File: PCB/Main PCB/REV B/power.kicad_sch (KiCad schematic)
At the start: 16 parts, among them U5 TPS2115APWR, U6 AMS1117-3.3

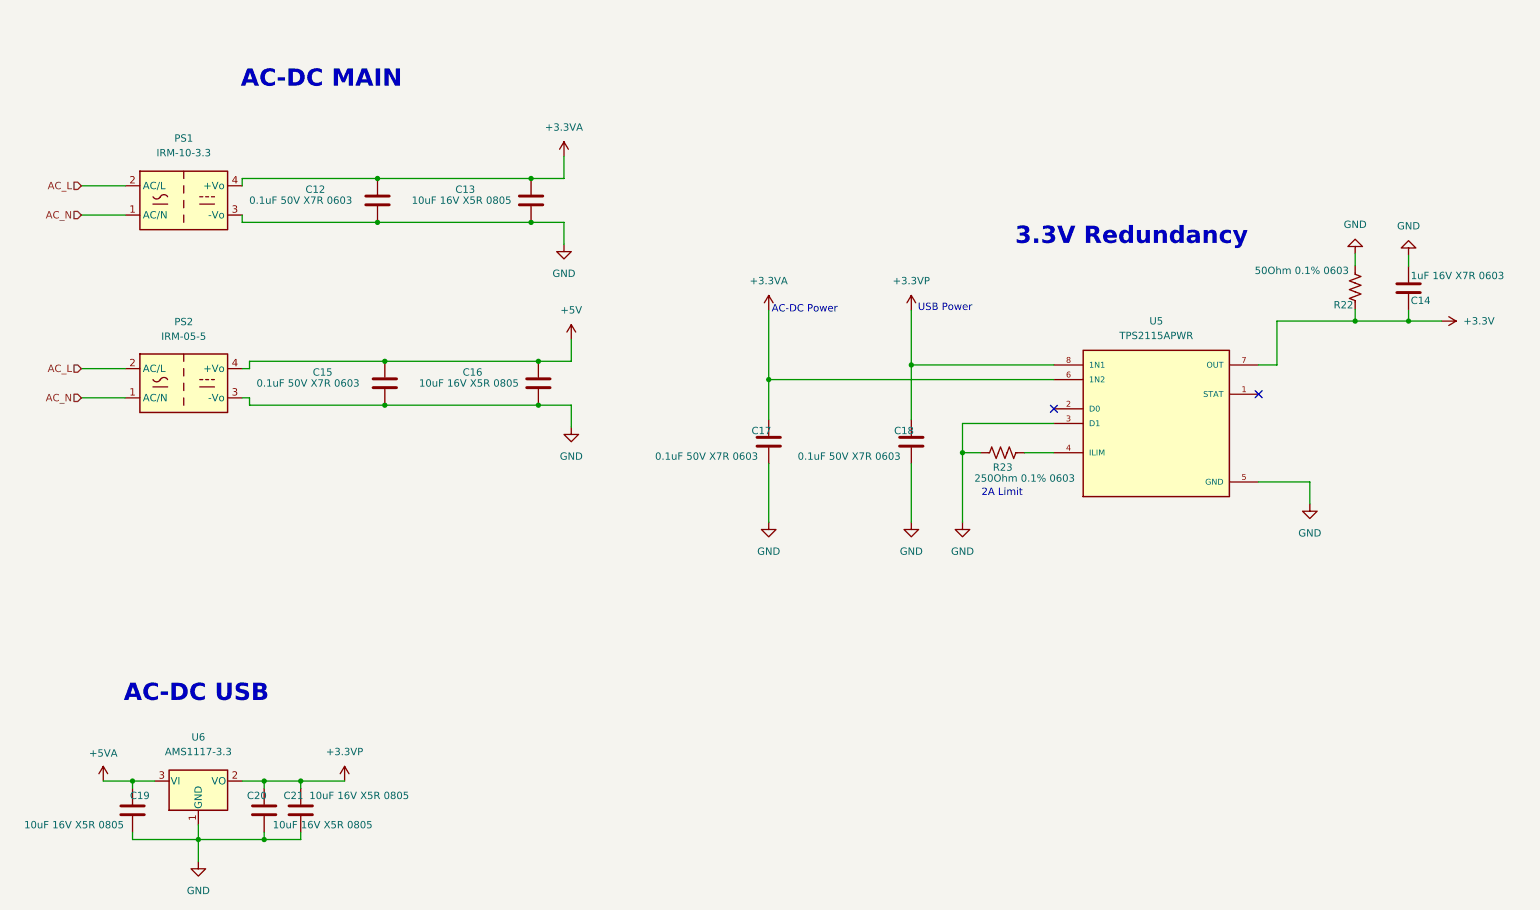
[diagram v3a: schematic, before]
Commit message: PCB schematic updates, Change to smaller thermocouple mux
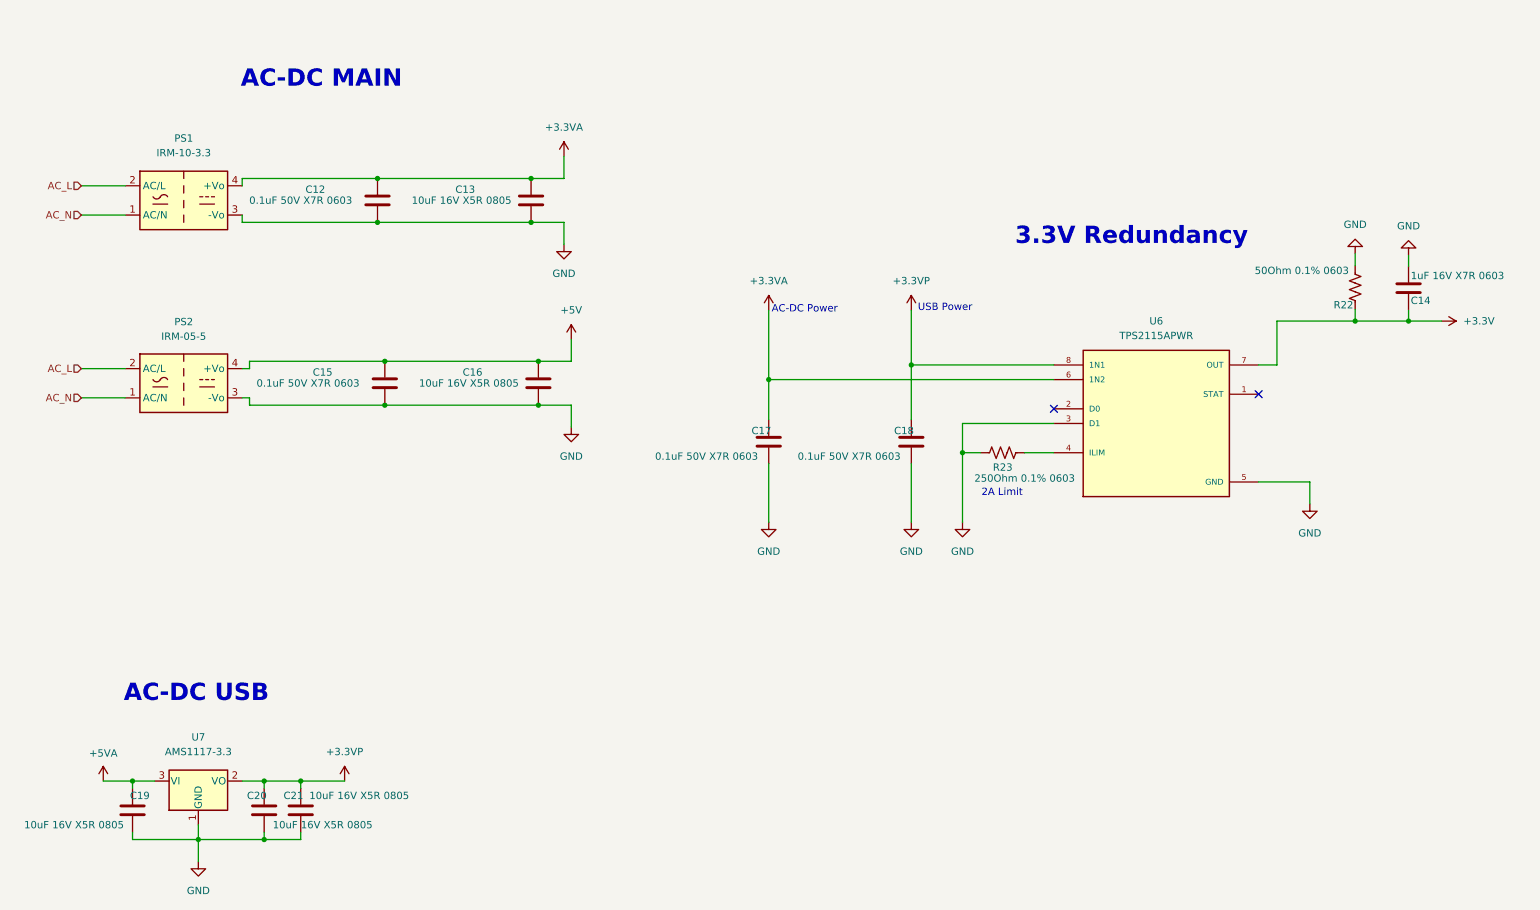
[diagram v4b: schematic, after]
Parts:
- renumbered U5 to U6, U6 to U7
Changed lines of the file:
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@@
   (symbol (lib_id "TPS2115APWR:TPS2115APWR") (at 218.694 92.329 0) (unit 1)
     (in_bom yes) (on_board yes) (fields_autoplaced)
-    (property "Reference" "U5" (id 0) (at 218.694 74.549 0))
+    (property "Reference" "U6" (id 0) (at 218.694 74.549 0))
     (property "Value" "TPS2115APWR" (id 1) (at 218.694 77.089 0))
     (property "Footprint" "Customs Smoker:PW8-M" (id 2) (at 218.694 92.329 0)
@@
   (symbol (lib_id "power:+3.3VP") (at 176.149 72.644 0) (unit 1)
     (in_bom yes) (on_board yes) (fields_autoplaced)
-    (property "Reference" "#PWR058" (id 0) (at 179.959 73.914 0)
+    (property "Reference" "#PWR057" (id 0) (at 179.959 73.914 0)
       (effects (font (size 1.27 1.27)) hide)
     )
@@
   (symbol (lib_id "power:GND") (at 52.324 168.402 0) (unit 1)
     (in_bom yes) (on_board yes)
-    (property "Reference" "#PWR068" (id 0) (at 52.324 174.752 0)
+    (property "Reference" "#PWR067" (id 0) (at 52.324 174.752 0)
       (effects (font (size 1.27 1.27)) hide)
     )
@@
   (symbol (lib_id "power:GND") (at 151.384 109.474 0) (unit 1)
     (in_bom yes) (on_board yes) (fields_autoplaced)
-    (property "Reference" "#PWR063" (id 0) (at 151.384 115.824 0)
+    (property "Reference" "#PWR062" (id 0) (at 151.384 115.824 0)
       (effects (font (size 1.27 1.27)) hide)
     )
@@
   (symbol (lib_id "power:GND") (at 185.039 109.474 0) (unit 1)
     (in_bom yes) (on_board yes) (fields_autoplaced)
-    (property "Reference" "#PWR065" (id 0) (at 185.039 115.824 0)
+    (property "Reference" "#PWR064" (id 0) (at 185.039 115.824 0)
       (effects (font (size 1.27 1.27)) hide)
     )
@@
   (symbol (lib_id "power:+3.3V") (at 268.224 74.549 270) (unit 1)
     (in_bom yes) (on_board yes) (fields_autoplaced)
-    (property "Reference" "#PWR059" (id 0) (at 264.414 74.549 0)
+    (property "Reference" "#PWR058" (id 0) (at 264.414 74.549 0)
       (effects (font (size 1.27 1.27)) hide)
     )
@@
   (symbol (lib_id "power:GND") (at 117.094 92.964 0) (unit 1)
     (in_bom yes) (on_board yes)
-    (property "Reference" "#PWR061" (id 0) (at 117.094 99.314 0)
+    (property "Reference" "#PWR060" (id 0) (at 117.094 99.314 0)
       (effects (font (size 1.27 1.27)) hide)
     )
@@
   (symbol (lib_id "power:+3.3VA") (at 151.384 72.644 0) (unit 1)
     (in_bom yes) (on_board yes) (fields_autoplaced)
-    (property "Reference" "#PWR057" (id 0) (at 151.384 76.454 0)
+    (property "Reference" "#PWR056" (id 0) (at 151.384 76.454 0)
       (effects (font (size 1.27 1.27)) hide)
     )
@@
   (symbol (lib_id "power:GND") (at 115.824 61.214 0) (unit 1)
     (in_bom yes) (on_board yes)
-    (property "Reference" "#PWR054" (id 0) (at 115.824 67.564 0)
+    (property "Reference" "#PWR053" (id 0) (at 115.824 67.564 0)
       (effects (font (size 1.27 1.27)) hide)
     )
@@
   (symbol (lib_id "power:GND") (at 253.238 62.865 180) (unit 1)
     (in_bom yes) (on_board yes) (fields_autoplaced)
-    (property "Reference" "#PWR055" (id 0) (at 253.238 56.515 0)
+    (property "Reference" "#PWR054" (id 0) (at 253.238 56.515 0)
       (effects (font (size 1.27 1.27)) hide)
     )
@@
   (symbol (lib_id "power:+3.3VP") (at 77.724 154.432 0) (unit 1)
     (in_bom yes) (on_board yes) (fields_autoplaced)
-    (property "Reference" "#PWR067" (id 0) (at 81.534 155.702 0)
+    (property "Reference" "#PWR066" (id 0) (at 81.534 155.702 0)
       (effects (font (size 1.27 1.27)) hide)
     )
@@
   (symbol (lib_id "power:GND") (at 262.509 63.119 180) (unit 1)
     (in_bom yes) (on_board yes) (fields_autoplaced)
-    (property "Reference" "#PWR056" (id 0) (at 262.509 56.769 0)
+    (property "Reference" "#PWR055" (id 0) (at 262.509 56.769 0)
       (effects (font (size 1.27 1.27)) hide)
     )
@@
   (symbol (lib_id "Regulator_Linear:AMS1117-3.3") (at 52.324 154.432 0) (unit 1)
     (in_bom yes) (on_board yes) (fields_autoplaced)
-    (property "Reference" "U6" (id 0) (at 52.324 146.812 0))
+    (property "Reference" "U7" (id 0) (at 52.324 146.812 0))
     (property "Value" "AMS1117-3.3" (id 1) (at 52.324 149.352 0))
     (property "Footprint" "Package_TO_SOT_SMD:TO-252-2" (id 2) (at 52.324 149.352 0)
@@
   (symbol (lib_id "power:+5VA") (at 35.814 154.432 0) (unit 1)
     (in_bom yes) (on_board yes) (fields_autoplaced)
-    (property "Reference" "#PWR066" (id 0) (at 35.814 158.242 0)
+    (property "Reference" "#PWR065" (id 0) (at 35.814 158.242 0)
       (effects (font (size 1.27 1.27)) hide)
     )
@@
   (symbol (lib_id "power:GND") (at 245.364 106.299 0) (unit 1)
     (in_bom yes) (on_board yes) (fields_autoplaced)
-    (property "Reference" "#PWR062" (id 0) (at 245.364 112.649 0)
+    (property "Reference" "#PWR061" (id 0) (at 245.364 112.649 0)
       (effects (font (size 1.27 1.27)) hide)
     )
@@
   (symbol (lib_id "power:+5V") (at 117.094 77.724 0) (unit 1)
     (in_bom yes) (on_board yes) (fields_autoplaced)
-    (property "Reference" "#PWR060" (id 0) (at 117.094 81.534 0)
+    (property "Reference" "#PWR059" (id 0) (at 117.094 81.534 0)
       (effects (font (size 1.27 1.27)) hide)
     )
@@
   (symbol (lib_id "power:GND") (at 176.149 109.474 0) (unit 1)
     (in_bom yes) (on_board yes) (fields_autoplaced)
-    (property "Reference" "#PWR064" (id 0) (at 176.149 115.824 0)
+    (property "Reference" "#PWR063" (id 0) (at 176.149 115.824 0)
       (effects (font (size 1.27 1.27)) hide)
     )
@@
   (symbol (lib_id "power:+3.3VA") (at 115.824 45.974 0) (unit 1)
     (in_bom yes) (on_board yes) (fields_autoplaced)
-    (property "Reference" "#PWR053" (id 0) (at 115.824 49.784 0)
-      (effects (font (size 1.27 1.27)) hide)
-    )
+    (property "Reference" "#PWR052" (id 0) (at 115.824 49.784 0)
+      (effects (font (size 1.27 1.27)) hide)
+    )

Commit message: PCB schematic updates, Reboot circuit fixed
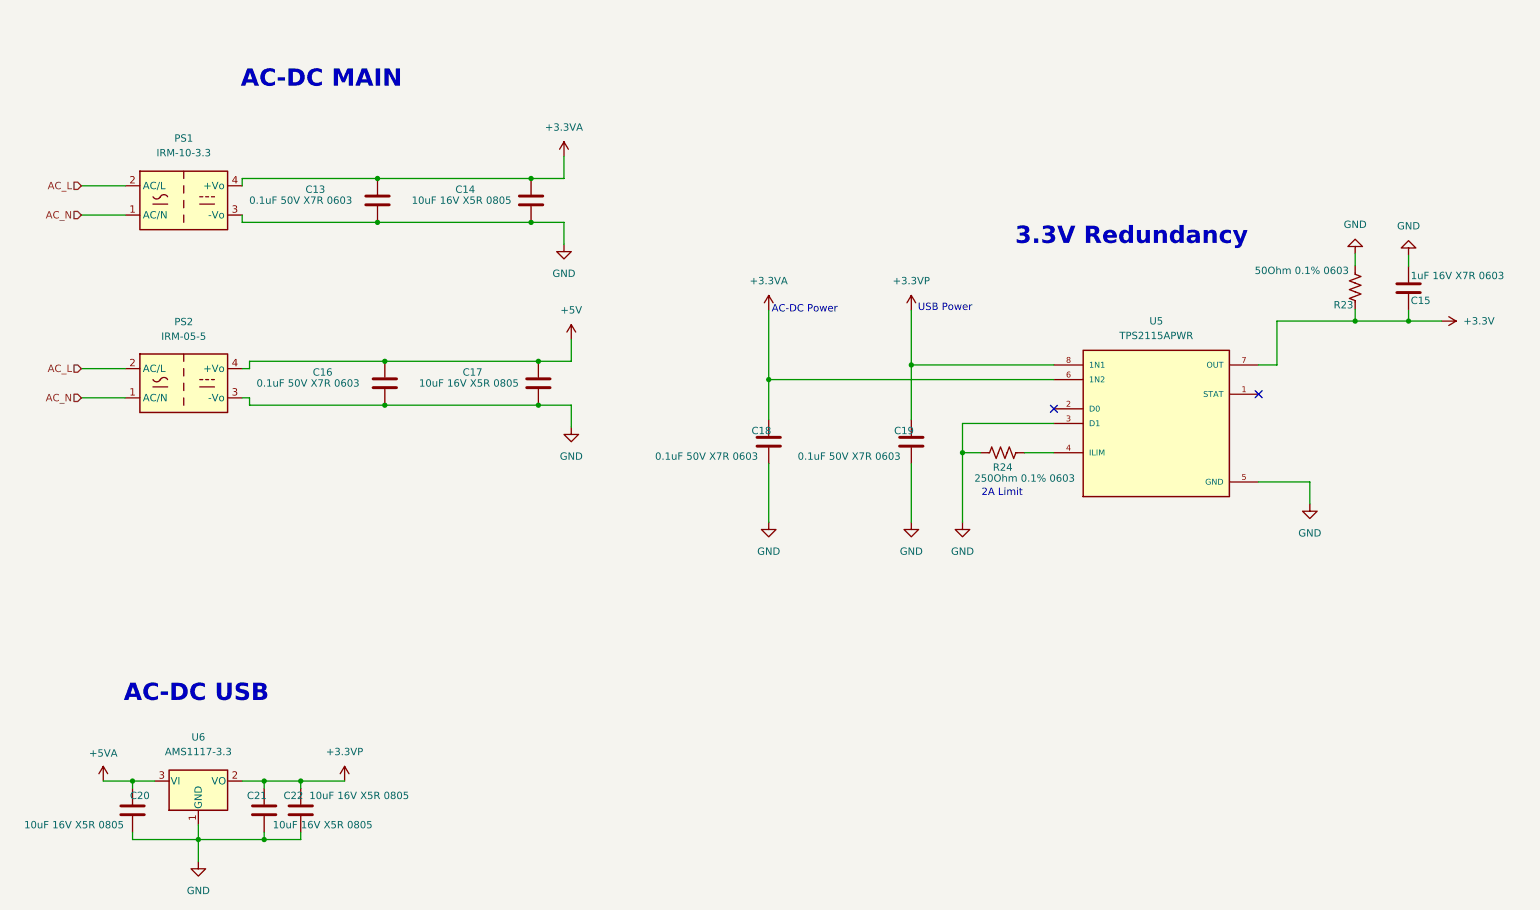
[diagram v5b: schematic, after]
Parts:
- renumbered C12 to C13, C13 to C14, C14 to C15, C15 to C16, C16 to C17, C17 to C18, C18 to C19, C19 to C20, C20 to C21, C21 to C22, R22 to R23, R23 to R24, U6 to U5, U7 to U6
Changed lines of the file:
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@@
 (kicad_sch (version 20211123) (generator eeschema)
-  (paper "A4")
+  (paper "A2")
   (junction (at 83.439 49.784) (diameter 0) (color 0 0 0 0)
   )
@@
   (symbol (lib_id "TPS2115APWR:TPS2115APWR") (at 218.694 92.329 0) (unit 1)
     (in_bom yes) (on_board yes) (fields_autoplaced)
-    (property "Reference" "U6" (id 0) (at 218.694 74.549 0))
+    (property "Reference" "U5" (id 0) (at 218.694 74.549 0))
     (property "Value" "TPS2115APWR" (id 1) (at 218.694 77.089 0))
     (property "Footprint" "Customs Smoker:PW8-M" (id 2) (at 218.694 92.329 0)
@@
   (symbol (lib_id "Device:C") (at 111.379 85.344 0) (mirror y) (unit 1)
     (in_bom yes) (on_board yes)
-    (property "Reference" "C16" (id 0) (at 99.949 83.439 0))
+    (property "Reference" "C17" (id 0) (at 99.949 83.439 0))
     (property "Value" "10uF 16V X5R 0805" (id 1) (at 99.314 85.344 0))
     (property "Footprint" "Capacitor_SMD:C_0805_2012Metric" (id 2) (at 110.4138 89.154 0)
@@
   (symbol (lib_id "Device:R_US") (at 253.238 68.707 0) (unit 1)
     (in_bom yes) (on_board yes)
-    (property "Reference" "R22" (id 0) (at 251.206 71.755 0))
+    (property "Reference" "R23" (id 0) (at 251.206 71.755 0))
     (property "Value" "50Ohm 0.1% 0603" (id 1) (at 243.967 65.786 0))
     (property "Footprint" "Resistor_SMD:R_0603_1608Metric" (id 2) (at 254.254 68.961 90)
@@
   (symbol (lib_id "Device:C") (at 110.109 53.594 0) (mirror y) (unit 1)
     (in_bom yes) (on_board yes)
-    (property "Reference" "C13" (id 0) (at 98.679 51.689 0))
+    (property "Reference" "C14" (id 0) (at 98.679 51.689 0))
     (property "Value" "10uF 16V X5R 0805" (id 1) (at 98.044 53.594 0))
     (property "Footprint" "Capacitor_SMD:C_0805_2012Metric" (id 2) (at 109.1438 57.404 0)
@@
   (symbol (lib_id "Device:R_US") (at 192.024 97.409 270) (unit 1)
     (in_bom yes) (on_board yes)
-    (property "Reference" "R23" (id 0) (at 192.024 99.949 90))
+    (property "Reference" "R24" (id 0) (at 192.024 99.949 90))
     (property "Value" "250Ohm 0.1% 0603" (id 1) (at 195.834 101.854 90))
     (property "Footprint" "Resistor_SMD:R_0603_1608Metric" (id 2) (at 191.77 98.425 90)
@@
   (symbol (lib_id "Device:C") (at 176.149 95.504 0) (mirror x) (unit 1)
     (in_bom yes) (on_board yes)
-    (property "Reference" "C18" (id 0) (at 174.879 93.599 0))
+    (property "Reference" "C19" (id 0) (at 174.879 93.599 0))
     (property "Value" "0.1uF 50V X7R 0603" (id 1) (at 165.354 98.044 0))
     (property "Footprint" "Capacitor_SMD:C_0603_1608Metric" (id 2) (at 177.1142 91.694 0)
@@
   (symbol (lib_id "Device:C") (at 63.754 159.512 0) (mirror y) (unit 1)
     (in_bom yes) (on_board yes)
-    (property "Reference" "C20" (id 0) (at 62.484 156.972 0))
+    (property "Reference" "C21" (id 0) (at 62.484 156.972 0))
     (property "Value" "10uF 16V X5R 0805" (id 1) (at 73.914 162.052 0))
     (property "Footprint" "Capacitor_SMD:C_0805_2012Metric" (id 2) (at 62.7888 163.322 0)
@@
   (symbol (lib_id "Device:C") (at 40.894 159.512 0) (unit 1)
     (in_bom yes) (on_board yes)
-    (property "Reference" "C19" (id 0) (at 42.164 156.972 0))
+    (property "Reference" "C20" (id 0) (at 42.164 156.972 0))
     (property "Value" "10uF 16V X5R 0805" (id 1) (at 30.734 162.052 0))
     (property "Footprint" "Capacitor_SMD:C_0805_2012Metric" (id 2) (at 41.8592 163.322 0)
@@
   (symbol (lib_id "Device:C") (at 70.104 159.512 0) (mirror y) (unit 1)
     (in_bom yes) (on_board yes)
-    (property "Reference" "C21" (id 0) (at 68.834 156.972 0))
+    (property "Reference" "C22" (id 0) (at 68.834 156.972 0))
     (property "Value" "10uF 16V X5R 0805" (id 1) (at 80.264 156.972 0))
     (property "Footprint" "Capacitor_SMD:C_0805_2012Metric" (id 2) (at 69.1388 163.322 0)
@@
   (symbol (lib_id "Device:C") (at 151.384 95.504 0) (mirror x) (unit 1)
     (in_bom yes) (on_board yes)
-    (property "Reference" "C17" (id 0) (at 150.114 93.599 0))
+    (property "Reference" "C18" (id 0) (at 150.114 93.599 0))
     (property "Value" "0.1uF 50V X7R 0603" (id 1) (at 140.589 98.044 0))
     (property "Footprint" "Capacitor_SMD:C_0603_1608Metric" (id 2) (at 152.3492 91.694 0)
@@
   (symbol (lib_id "Device:C") (at 84.709 85.344 0) (mirror x) (unit 1)
     (in_bom yes) (on_board yes)
-    (property "Reference" "C15" (id 0) (at 73.914 83.439 0))
+    (property "Reference" "C16" (id 0) (at 73.914 83.439 0))
     (property "Value" "0.1uF 50V X7R 0603" (id 1) (at 71.374 85.344 0))
     (property "Footprint" "Capacitor_SMD:C_0603_1608Metric" (id 2) (at 85.6742 81.534 0)
@@
   (symbol (lib_id "Regulator_Linear:AMS1117-3.3") (at 52.324 154.432 0) (unit 1)
     (in_bom yes) (on_board yes) (fields_autoplaced)
-    (property "Reference" "U7" (id 0) (at 52.324 146.812 0))
+    (property "Reference" "U6" (id 0) (at 52.324 146.812 0))
     (property "Value" "AMS1117-3.3" (id 1) (at 52.324 149.352 0))
     (property "Footprint" "Package_TO_SOT_SMD:TO-252-2" (id 2) (at 52.324 149.352 0)
@@
   (symbol (lib_id "Device:C") (at 262.509 68.834 0) (unit 1)
     (in_bom yes) (on_board yes)
-    (property "Reference" "C14" (id 0) (at 262.89 70.993 0)
+    (property "Reference" "C15" (id 0) (at 262.89 70.993 0)
       (effects (font (size 1.27 1.27)) (justify left))
     )
@@
   (symbol (lib_id "Device:C") (at 83.439 53.594 0) (mirror x) (unit 1)
     (in_bom yes) (on_board yes)
-    (property "Reference" "C12" (id 0) (at 72.644 51.689 0))
+    (property "Reference" "C13" (id 0) (at 72.644 51.689 0))
     (property "Value" "0.1uF 50V X7R 0603" (id 1) (at 70.104 53.594 0))
     (property "Footprint" "Capacitor_SMD:C_0603_1608Metric" (id 2) (at 84.4042 49.784 0)
